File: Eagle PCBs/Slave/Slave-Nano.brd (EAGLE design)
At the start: 66.1 x 67.5 mm, 15 parts, among them Q1 TIP120

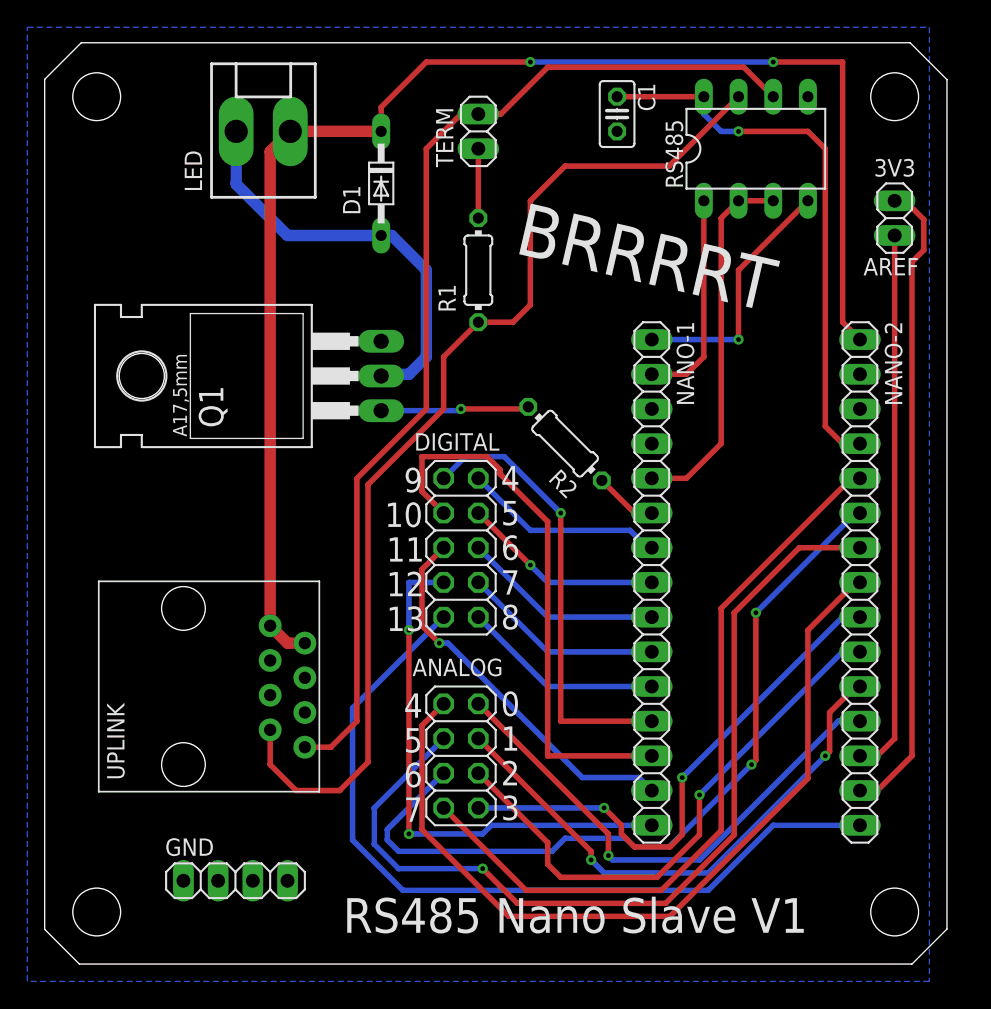
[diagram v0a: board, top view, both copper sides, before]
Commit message: Minor PCB adjustments
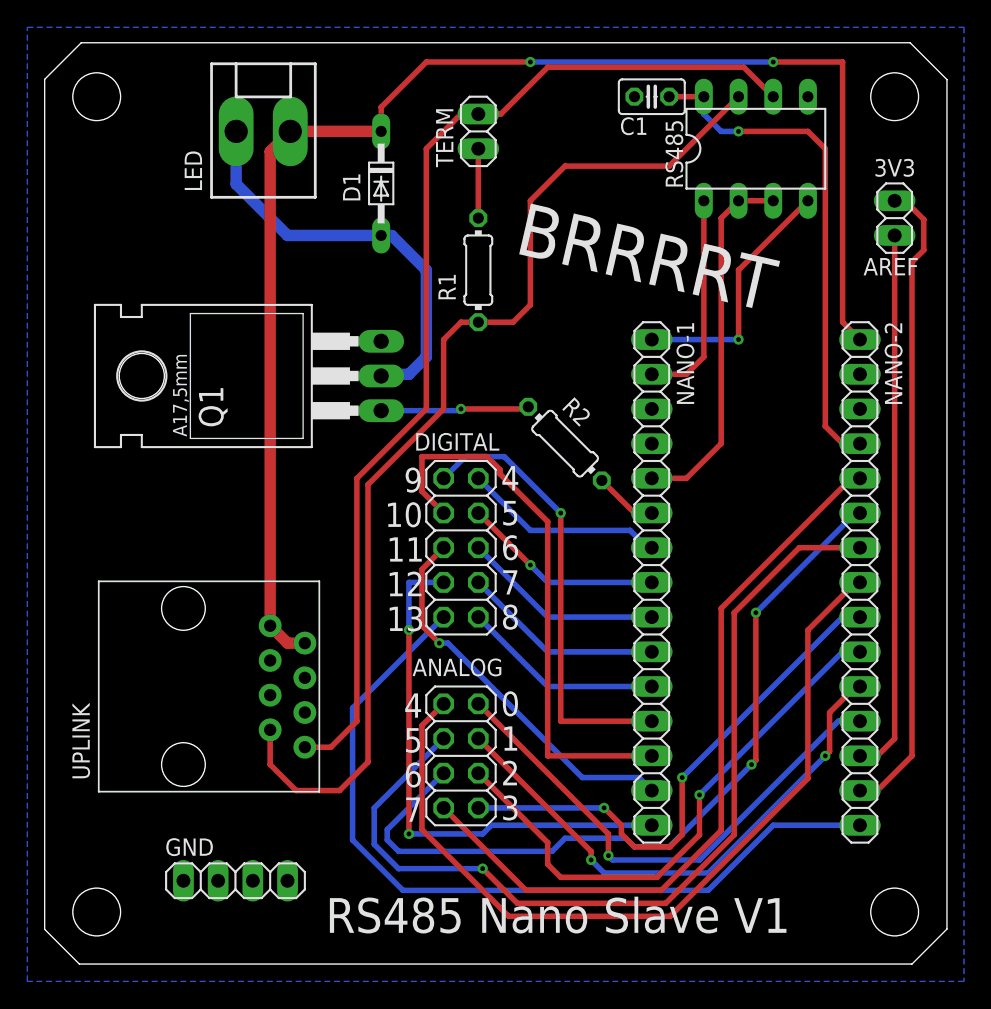
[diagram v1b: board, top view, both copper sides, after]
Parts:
- moved C1 2.84 mm to (44.5, 63.5), turned to 180 degrees
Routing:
- net 5VCC: track 40.9 -> 37.1 mm
- net RS485_B: track 77.3 -> 78.0 mm
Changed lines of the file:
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@@
 <hole x="62.23" y="3.81" drill="3.5"/>
 <hole x="3.81" y="3.81" drill="3.5"/>
-<text x="21.844" y="2.286" size="2.54" layer="25">RS485 Nano Slave V1</text>
+<text x="20.574" y="2.286" size="2.54" layer="25">RS485 Nano Slave V1</text>
 <text x="33.401" y="34.671" size="1.778" layer="25">4</text>
 <text x="33.401" y="32.131" size="1.778" layer="25">5</text>
@@
 </autorouter>
 <elements>
-<element name="C1" library="rcl" library_urn="urn:adsk.eagle:library:334" package="C025-025X050" package3d_urn="urn:adsk.eagle:package:23629/2" value="0.1uF" x="41.91" y="62.23" smashed="yes" rot="R270">
-<attribute name="NAME" x="43.434" y="64.516" size="1.27" layer="25" ratio="10" rot="R270"/>
-<attribute name="POPULARITY" value="65" x="12.7" y="45.72" size="1.778" layer="27" rot="R270" display="off"/>
-<attribute name="SPICEPREFIX" value="C" x="12.7" y="45.72" size="1.778" layer="27" rot="R270" display="off"/>
-<attribute name="VALUE" x="39.116" y="64.516" size="1.27" layer="27" ratio="10" rot="R270"/>
+<element name="C1" library="rcl" library_urn="urn:adsk.eagle:library:334" package="C025-025X050" package3d_urn="urn:adsk.eagle:package:23629/2" value="0.1uF" x="44.45" y="63.5" smashed="yes" rot="R180">
+<attribute name="NAME" x="44.196" y="61.976" size="1.27" layer="25" ratio="10" rot="R180"/>
+<attribute name="POPULARITY" value="65" x="27.94" y="92.71" size="1.778" layer="27" rot="R180" display="off"/>
+<attribute name="SPICEPREFIX" value="C" x="27.94" y="92.71" size="1.778" layer="27" rot="R180" display="off"/>
+<attribute name="VALUE" x="46.736" y="66.294" size="1.27" layer="27" ratio="10" rot="R180"/>
 </element>
 <element name="RS485" library="A10 Library" package="DIL08" package3d_urn="urn:adsk.eagle:package:29519/2" value="MAX487CPA" x="52.07" y="59.69" smashed="yes">
@@
 </element>
 <element name="R1" library="rcl" library_urn="urn:adsk.eagle:library:334" package="0204/7" package3d_urn="urn:adsk.eagle:package:23498/2" value="120Ω" x="31.75" y="50.8" smashed="yes" rot="R270">
-<attribute name="NAME" x="28.829" y="49.784" size="1.27" layer="25" ratio="10" rot="R270"/>
+<attribute name="NAME" x="30.099" y="48.514" size="1.27" layer="25" ratio="10" rot="R90"/>
 <attribute name="POPULARITY" value="79" x="31.75" y="50.8" size="1.778" layer="27" rot="R270" display="off"/>
 <attribute name="SPICEPREFIX" value="R" x="31.75" y="50.8" size="1.778" layer="27" rot="R270" display="off"/>
@@
 </element>
 <element name="R2" library="rcl" library_urn="urn:adsk.eagle:library:334" package="0204/7" package3d_urn="urn:adsk.eagle:package:23498/2" value="1K" x="38.1" y="38.1" smashed="yes" rot="R135">
-<attribute name="NAME" x="39.17763125" y="34.86710625" size="1.27" layer="25" ratio="10" rot="R135"/>
+<attribute name="NAME" x="37.78063125" y="40.70910625" size="1.27" layer="25" ratio="10" rot="R315"/>
 <attribute name="POPULARITY" value="79" x="11.159234375" y="11.15923125" size="1.778" layer="27" rot="R135" display="off"/>
 <attribute name="SPICEPREFIX" value="R" x="11.159234375" y="11.15923125" size="1.778" layer="27" rot="R135" display="off"/>
@@
 <attribute name="NAME" x="13.081" y="39.243" size="1.778" layer="25" ratio="10" rot="R90"/>
 <attribute name="POPULARITY" value="2" x="-2.032" y="30.353" size="1.778" layer="27" rot="R90" display="off"/>
-<attribute name="VALUE" x="15.748" y="39.116" size="1.778" layer="27" ratio="10" rot="R90"/>
+<attribute name="VALUE" x="18.288" y="39.116" size="1.778" layer="27" ratio="10" rot="R90"/>
 </element>
 <element name="LED" library="con-molex" library_urn="urn:adsk.eagle:library:165" package="KK-156-2" package3d_urn="urn:adsk.eagle:package:8078800/1" value="" x="16.002" y="60.96" smashed="yes">
@@
 </element>
 <element name="D1" library="diode" library_urn="urn:adsk.eagle:library:210" package="DO34-7" package3d_urn="urn:adsk.eagle:package:43348/1" value="BAT81" x="24.638" y="57.15" smashed="yes" rot="R270">
-<attribute name="NAME" x="21.844" y="57.023" size="1.27" layer="25" ratio="10" rot="R270"/>
+<attribute name="NAME" x="23.114" y="55.753" size="1.27" layer="25" ratio="10" rot="R90"/>
 <attribute name="POPULARITY" value="5" x="24.638" y="57.15" size="1.778" layer="27" rot="R270" display="off"/>
 <attribute name="VALUE" x="21.844" y="59.182" size="1.27" layer="27" ratio="10" rot="R270" display="off"/>
 </element>
 <element name="UPLINK" library="A10 Library" package="RJ45-8P8C" value="RJ45-8P8C" x="10.16" y="20.32" smashed="yes" rot="R90">
-<attribute name="NAME" x="5.842" y="13.462" size="1.27" layer="25" rot="R90"/>
+<attribute name="NAME" x="3.302" y="13.462" size="1.27" layer="25" rot="R90"/>
 <attribute name="VALUE" x="8.89" y="15.24" size="1.27" layer="27" rot="R90" display="off"/>
 </element>
@@
 <polygon width="0.8128" layer="16">
 <vertex x="-1.27" y="68.58"/>
-<vertex x="64.77" y="68.58"/>
-<vertex x="64.77" y="-1.27"/>
+<vertex x="67.31" y="68.58"/>
+<vertex x="67.31" y="-1.27"/>
 <vertex x="-1.27" y="-1.27"/>
 </polygon>
@@
 <wire x1="35.56" y1="48.26" x2="34.29" y2="46.99" width="0.4064" layer="1"/>
 <wire x1="34.29" y1="46.99" x2="31.75" y2="46.99" width="0.4064" layer="1"/>
-<wire x1="31.75" y1="46.99" x2="29.21" y2="44.45" width="0.4064" layer="1"/>
-<wire x1="29.21" y1="44.45" x2="29.21" y2="40.64" width="0.4064" layer="1"/>
+<wire x1="31.75" y1="46.99" x2="30.48" y2="46.99" width="0.4064" layer="1"/>
+<wire x1="30.48" y1="46.99" x2="29.21" y2="45.72" width="0.4064" layer="1"/>
+<wire x1="29.21" y1="45.72" x2="29.21" y2="40.64" width="0.4064" layer="1"/>
 <wire x1="18.415" y1="12.7" x2="21.59" y2="12.7" width="0.4064" layer="1"/>
 <wire x1="21.59" y1="12.7" x2="23.6728" y2="14.7828" width="0.4064" layer="1"/>
@@
 <contactref element="RS485" pad="8"/>
 <contactref element="NANO-2" pad="4"/>
-<wire x1="48.26" y1="63.5" x2="41.91" y2="63.5" width="0.4064" layer="1"/>
+<wire x1="48.26" y1="63.5" x2="45.72" y2="63.5" width="0.4064" layer="1"/>
 <wire x1="59.69" y1="38.1" x2="58.42" y2="38.1" width="0.4064" layer="1"/>
 <wire x1="58.42" y1="38.1" x2="57.15" y2="39.37" width="0.4064" layer="1"/>

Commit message: Minor PCB adjustments
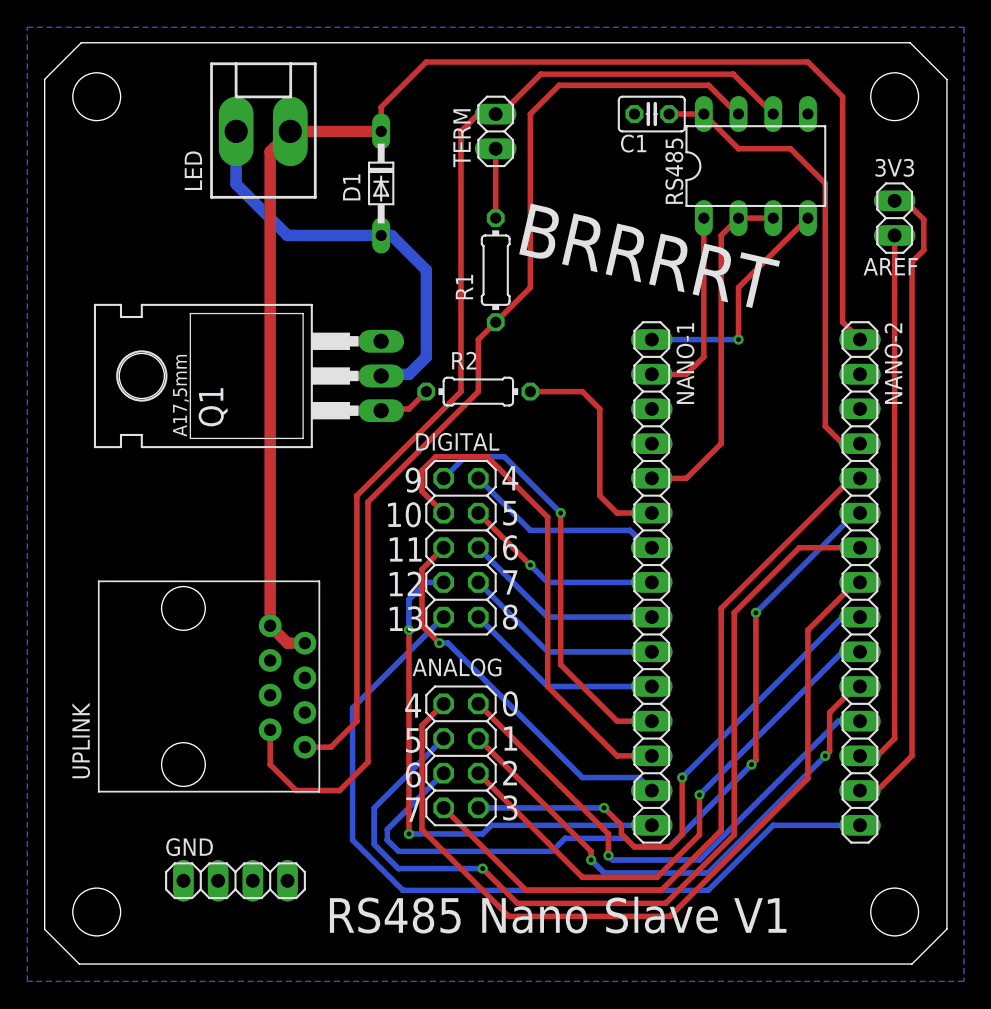
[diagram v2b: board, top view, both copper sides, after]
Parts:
- moved R2 7.41 mm to (31.8, 41.9), turned to 180 degrees
- moved C1 1.27 mm to (44.5, 62.2)
- moved R1 1.27 mm to (33.0, 50.8)
- moved TERM 1.27 mm to (33.0, 61.0)
- moved RS485 1.27 mm to (52.1, 58.4)
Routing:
- net NANO_D3: track 4.64 -> 16.3 mm
- net LED_PWM: track 11.0 -> 3.88 mm, vias 1 -> 0
- net D10: track 40.9 -> 37.3 mm
- net 5VCC: track 37.1 -> 34.4 mm, vias 1 -> 0
- net RS485_B: track 78.0 -> 80.7 mm
- net D9: track 32.8 -> 30.4 mm
- net VDD: track 104.3 -> 102.8 mm, vias 2 -> 0
- net NANO_RX: track 15.8 -> 14.5 mm
- net NANO_TX: track 18.6 -> 17.3 mm
- net NANO_D2: track 27.0 -> 25.7 mm
- net A2: track 40.6 -> 39.6 mm
- net D12: track 39.0 -> 38.3 mm
- net RS485_A: track 77.4 -> 76.7 mm

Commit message: Added a 5v bus to all PCBs
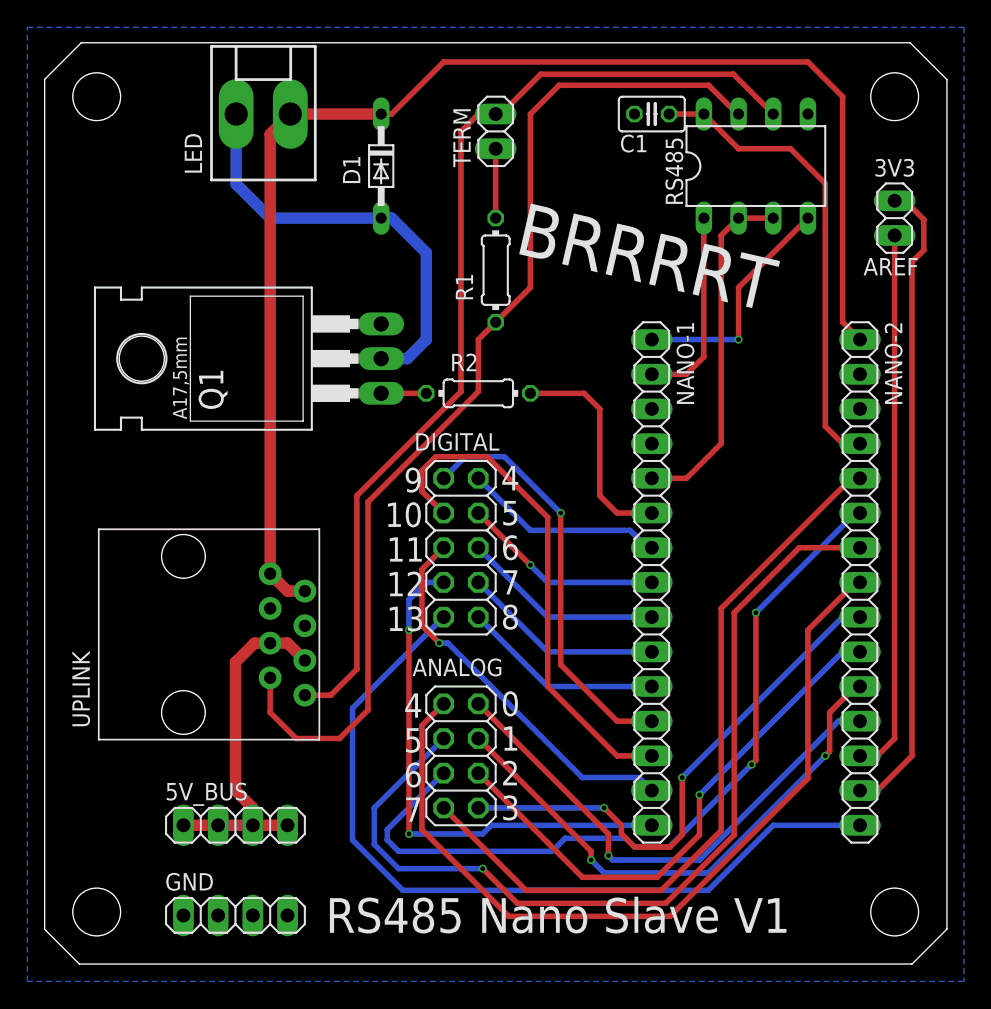
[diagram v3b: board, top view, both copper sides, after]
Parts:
- added 5V_BUS: (no value), pinhead:1X04
- moved UPLINK 3.81 mm to (10.2, 24.1)
- moved GND 2.54 mm to (14.0, 3.56)
- moved D1 1.27 mm to (24.6, 58.4)
- moved Q1 1.27 mm to (18.3, 44.3)
- moved LED 1.27 mm to (16.0, 62.2)
- moved R2 0.13 mm to (31.8, 41.8)
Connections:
- new net 5V_BUS: 5V_BUS.1, 5V_BUS.2, 5V_BUS.3, 5V_BUS.4, UPLINK.5, UPLINK.6
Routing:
- net 5V_BUS: track 0.00 -> 26.3 mm
- net VDD: track 102.8 -> 98.7 mm
- net RS485_B: track 80.7 -> 76.9 mm
- net RS485_A: track 76.7 -> 72.9 mm
- net LED_GND: track 30.6 -> 31.4 mm
- net LED_PWM: track 3.88 -> 3.30 mm
